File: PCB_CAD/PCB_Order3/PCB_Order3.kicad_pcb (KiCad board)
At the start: 4 copper layers, 150 x 130 mm, 95 parts

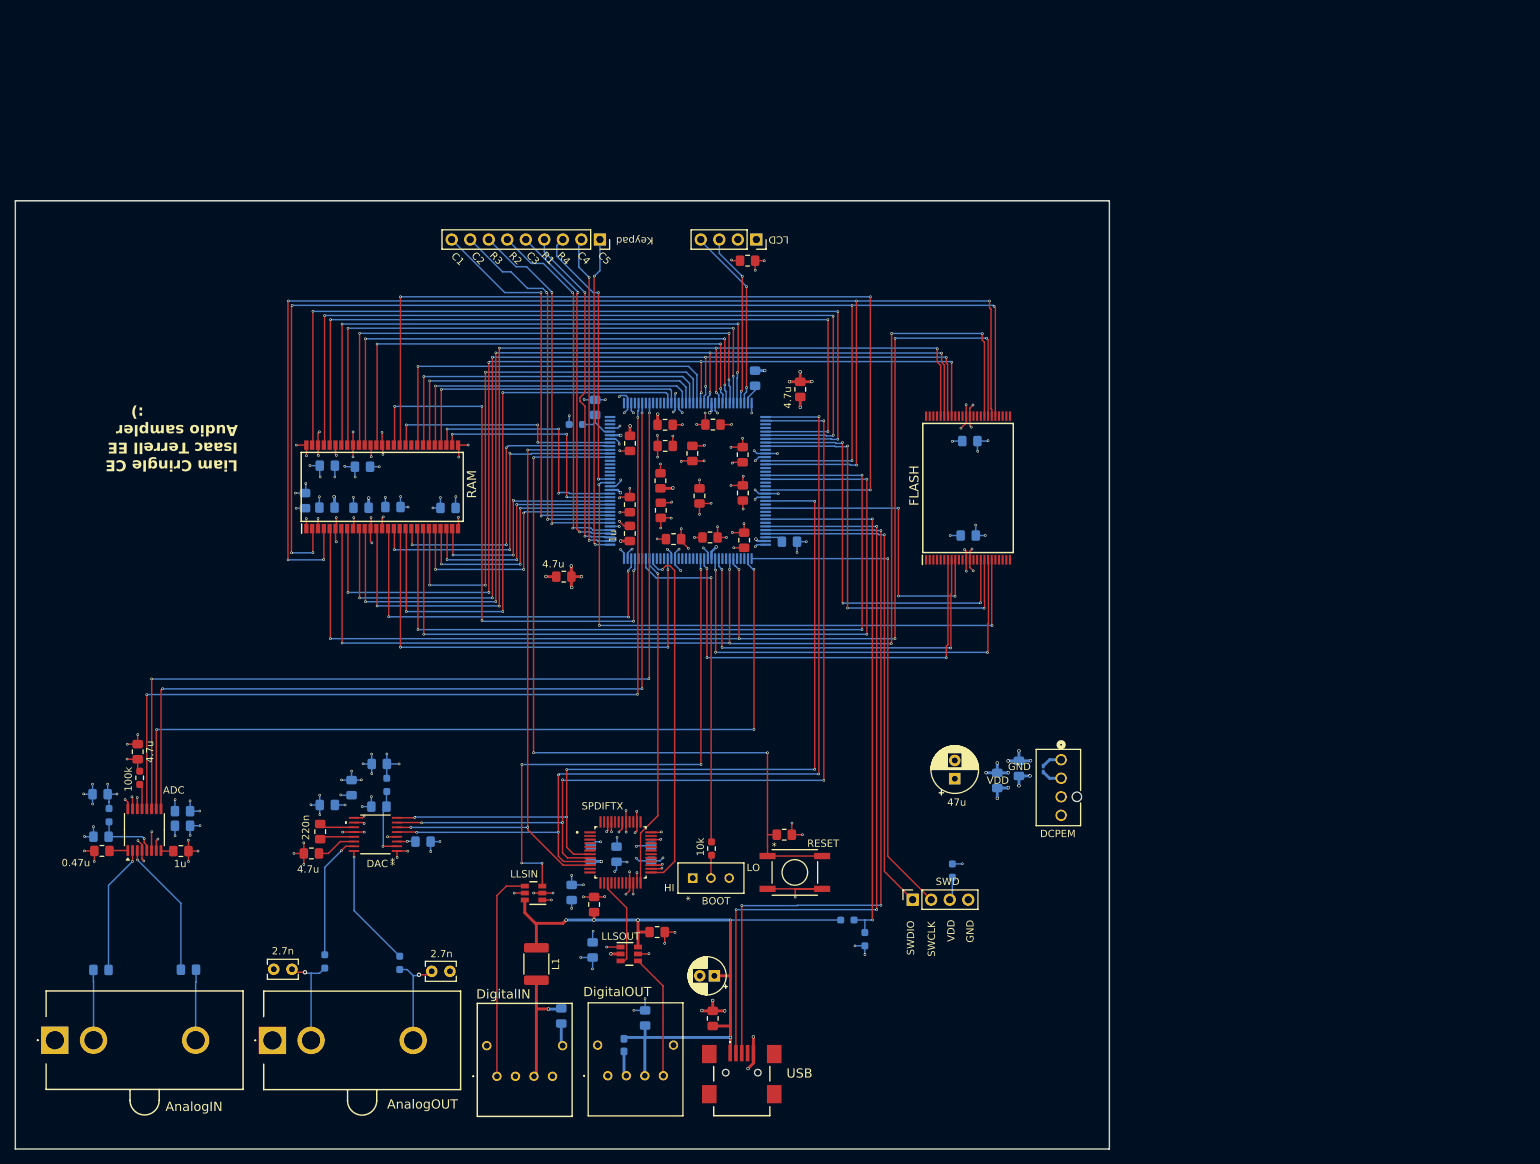
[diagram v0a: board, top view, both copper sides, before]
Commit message: fixed via size and clearance issues
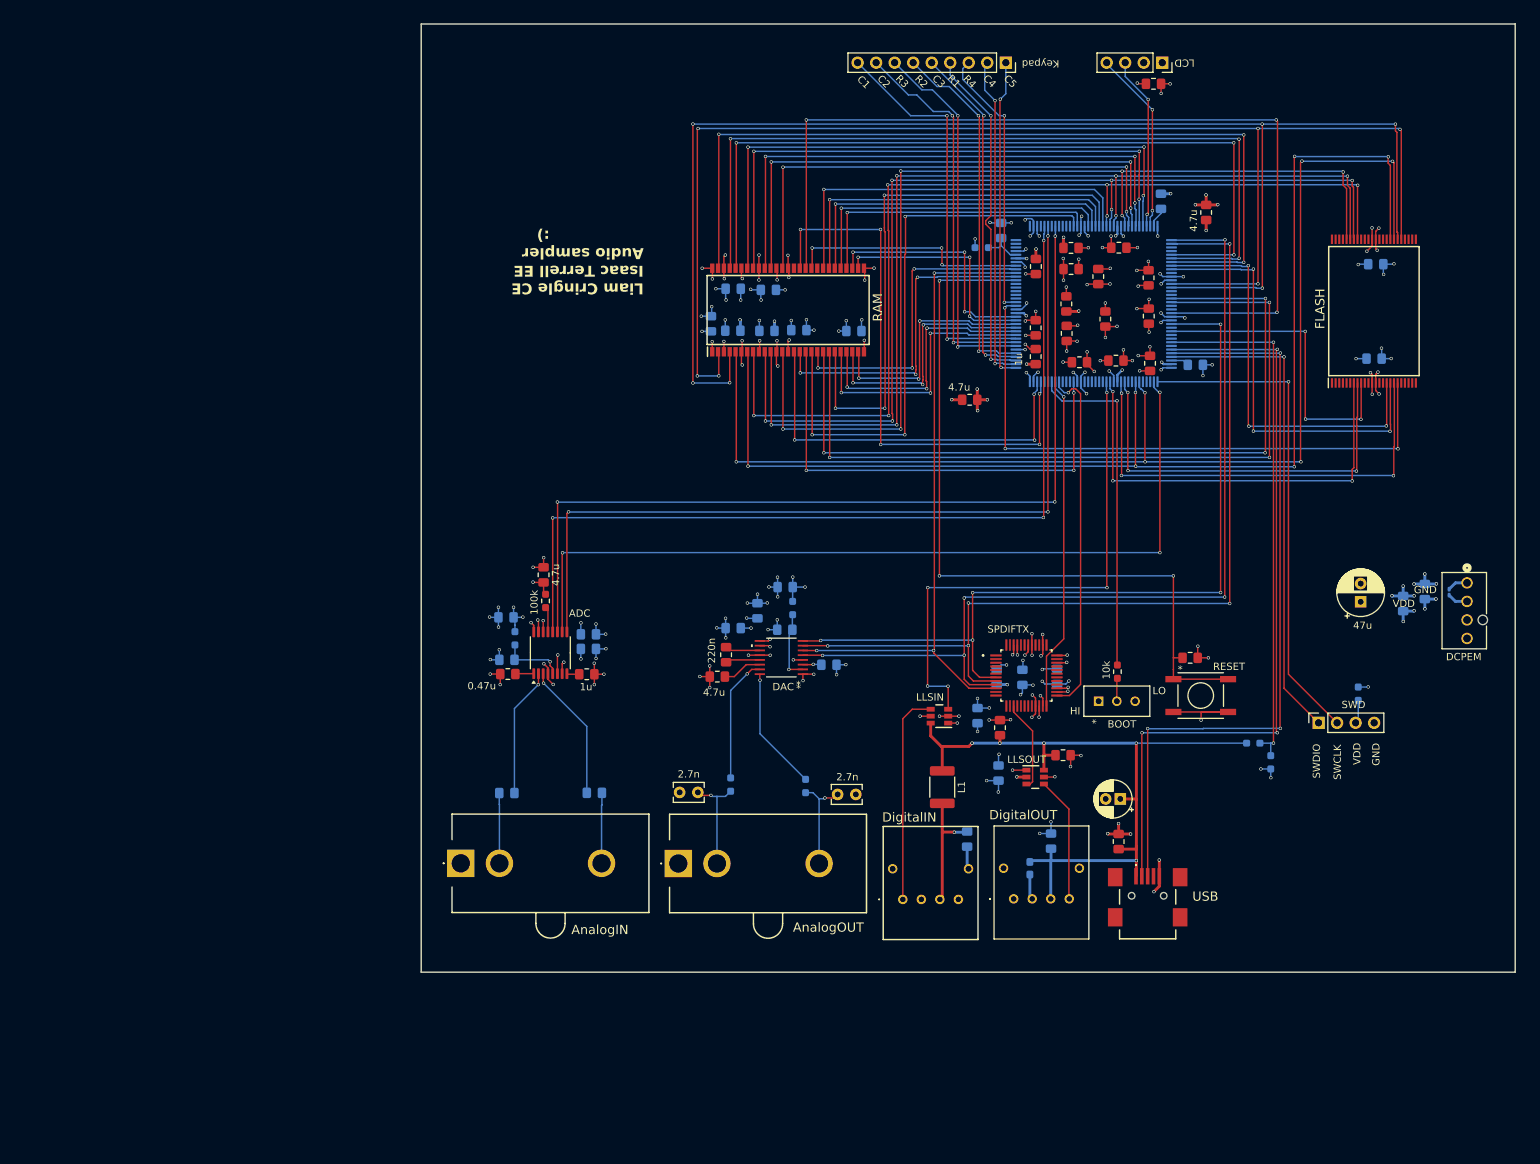
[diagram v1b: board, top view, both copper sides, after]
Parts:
- moved ADC 60.7 mm to (101.2, 107.1)
- moved ArC1 60.7 mm to (106.2, 110.0)
- moved BC1 60.7 mm to (188.9, 107.8)
- moved DacOut_R_res1 60.7 mm to (125.9, 125.2)
- moved LCD 60.7 mm to (185.1, 26.2)
- moved LLSIN 60.7 mm to (154.5, 115.8)
- moved MnC12 60.7 mm to (171.9, 59.3)
- moved MunC1 60.7 mm to (176.3, 55.5)
- moved AB1 60.7 mm to (96.3, 105.1)
- moved AR1 60.7 mm to (100.5, 100.0)
- moved AbC1 60.7 mm to (95.1, 102.2)
- moved AcC1 60.7 mm to (95.3, 110.0)
- moved AdbC1 60.7 mm to (95.2, 126.3)
- moved AdbC2 60.7 mm to (107.2, 126.3)
- moved AnC1 60.7 mm to (95.2, 108.1)
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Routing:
- net /USB_OTG_HS_DP: track 106.6 -> 104.9 mm
- net /USB_OTG_HS_VBUS: track 73.9 -> 72.5 mm
- net /USB_OTG_HS_DM: track 106.7 -> 105.4 mm
- net /FMC_BA1: track 110.5 -> 109.5 mm
- net /FMC_A2: track 34.2 -> 35.1 mm
- net /FMC_A1: track 35.7 -> 36.6 mm
- net /FMC_BA0: track 109.2 -> 108.4 mm
- net GNDD: track 278.2 -> 278.9 mm
- net /FMC_A3: track 32.8 -> 33.3 mm
- net /FMC_A0: track 37.4 -> 37.9 mm

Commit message: Our long national nightmare is over
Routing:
- net GNDD: vias 175 -> 184
- added copper zone on B.Cu, net GNDD
- added copper zone on F.Cu, net GNDD
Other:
- board text added: "0.47µ"
- board text added: "100k"
- board text added: "10k"
- board text added: "10µ"
- board text added: "1µ"
- board text added: "2.2µ"
- board text added: "2.7n"
- board text added: "220n"
- board text added: "33k"
- board text added: "4.7µ"
- board text added: "47µ"
- board text added: "5.6k"
- board text added: "510"
- board text added: "82k"
- board text added: "Liam Cringle CE Isaac Terrell EE Audio sampler )"
- board text added: "Unless otherwise noted, resistors & ferrite beads 0603, capacitors 0805 All capacitors not explicated are 0.1µ"
- board text removed: "Liam Cringle CE Isaac Terrell EE Audio sampler :)"
